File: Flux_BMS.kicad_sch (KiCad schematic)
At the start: 13 parts, among them Q1 BSS84, Q2 BSS84

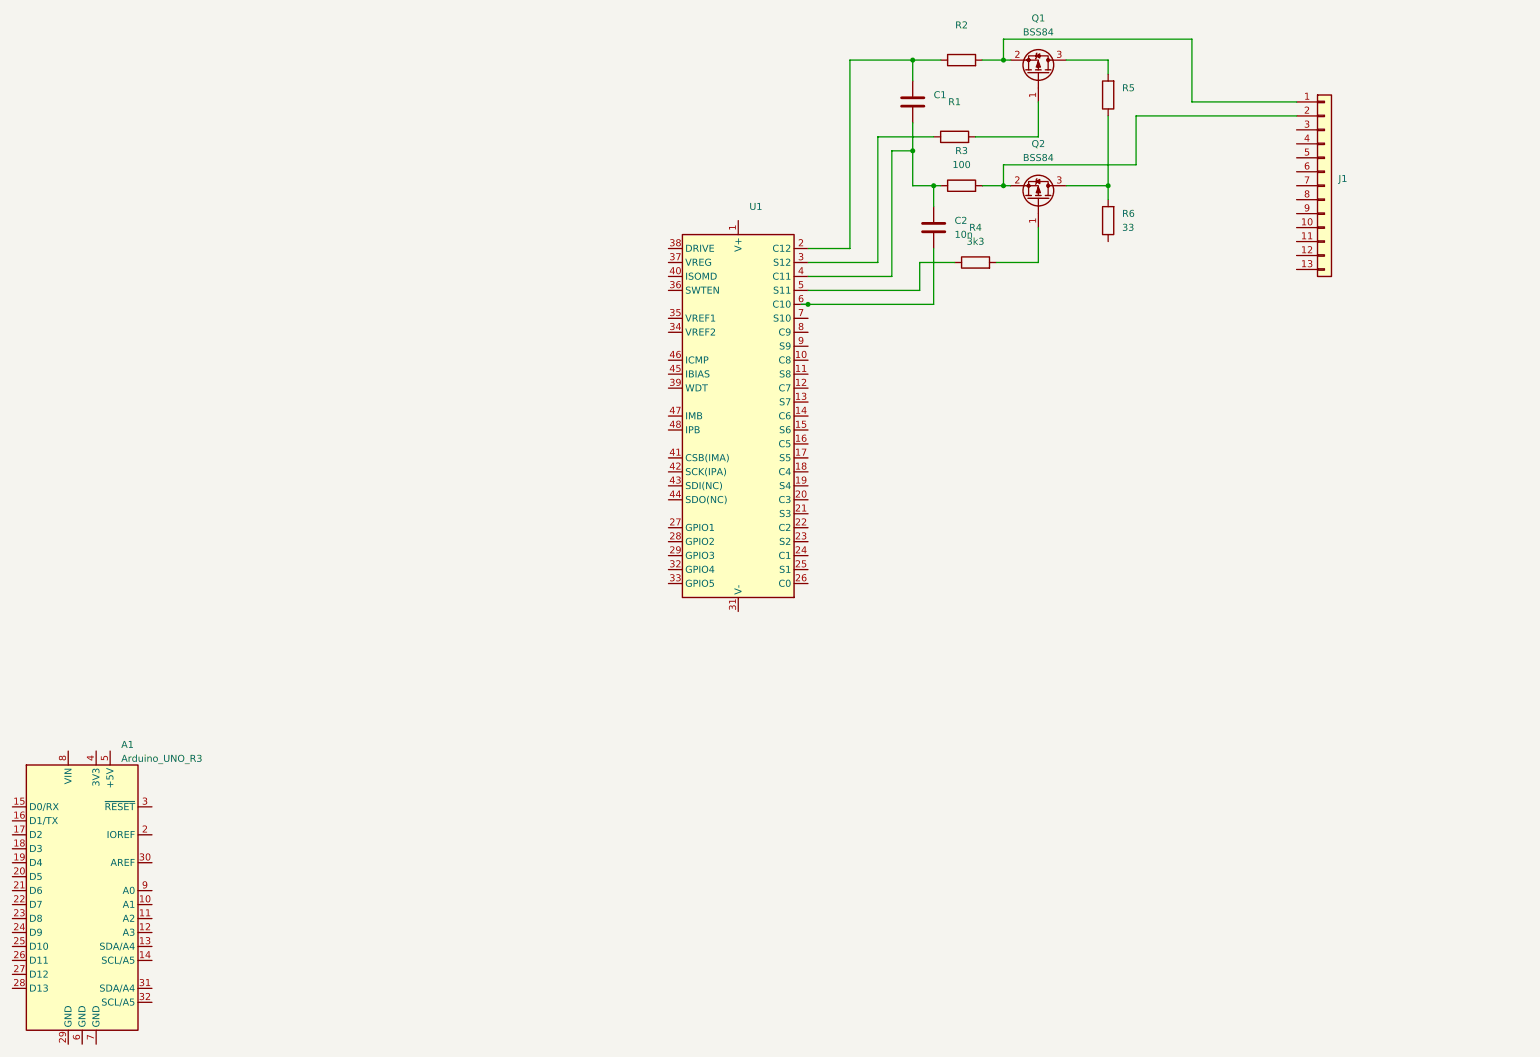
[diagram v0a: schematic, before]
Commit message: Added ltc6811
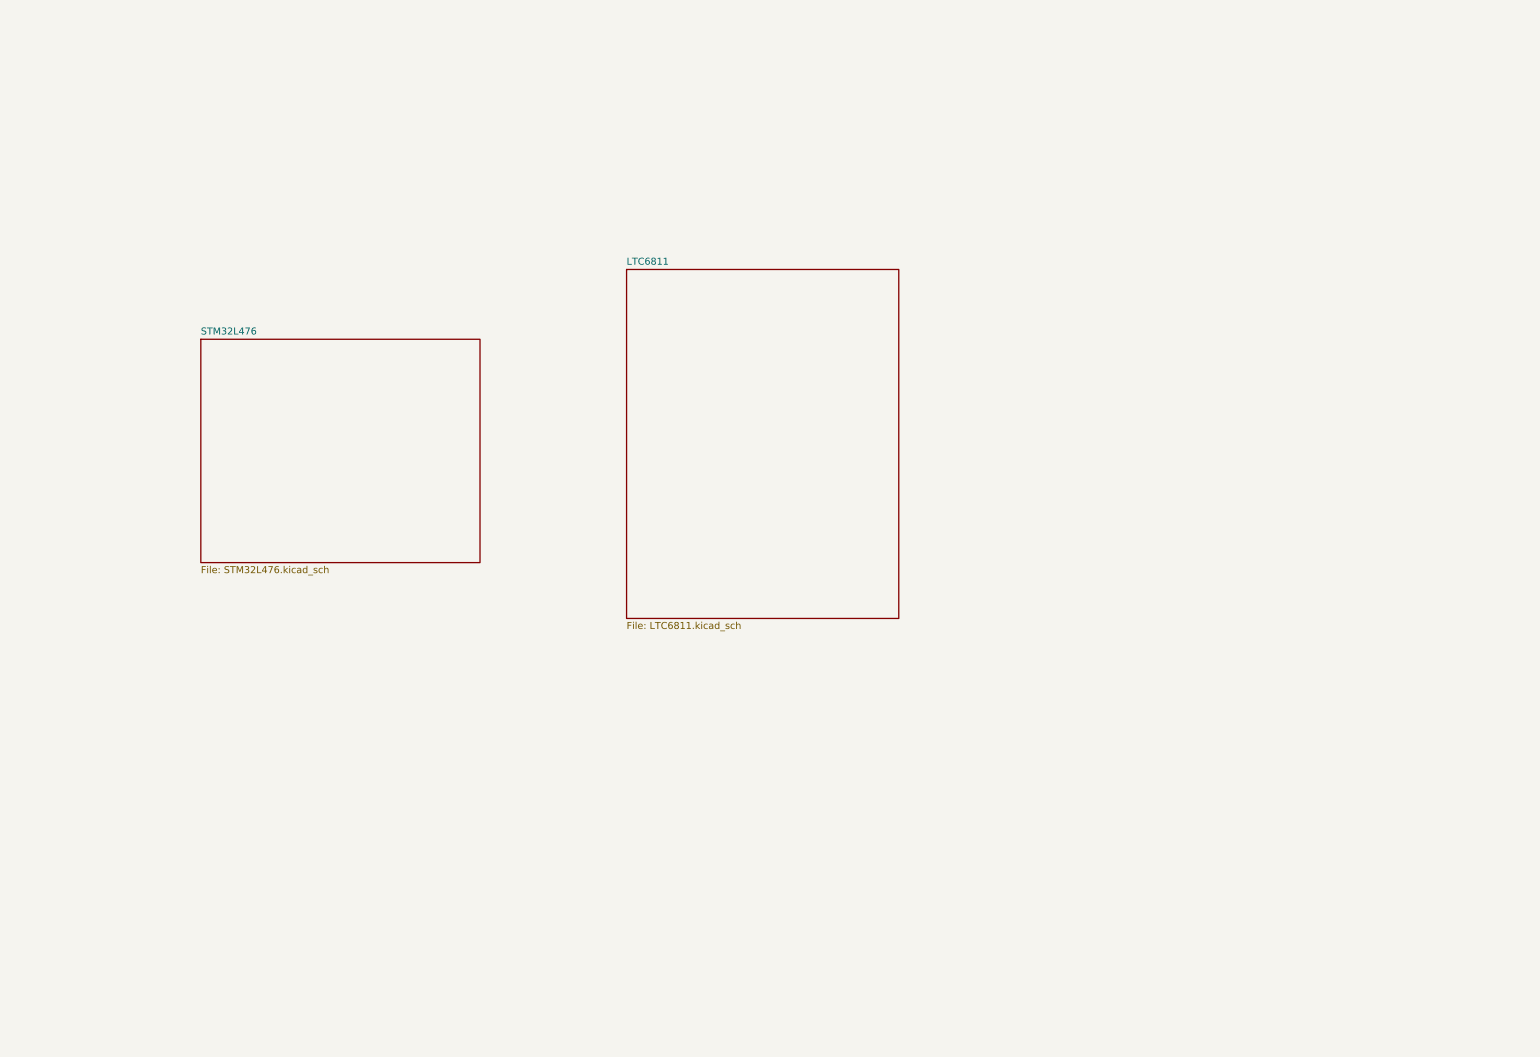
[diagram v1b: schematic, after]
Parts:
- removed A1: Arduino_UNO_R3, Module:Arduino_UNO_R3, symbol MCU_Module:Arduino_UNO_R3
- removed C1: (no value), symbol Device:C
- removed C2: 10n, Capacitor_SMD:C_0805_2012Metric_Pad1.18x1.45mm_HandSolder, symbol Device:C
- removed J1: (no value), symbol Connector_Generic:Conn_01x13
- removed Q1, Q2: BSS84, Package_TO_SOT_SMD:SOT-23, symbol Transistor_FET:BSS84
- removed R1, R5: (no value), Resistor_SMD:R_0805_2012Metric_Pad1.20x1.40mm_HandSolder, symbol Device:R
- removed R2: (no value), symbol Device:R
- removed R3: 100, Resistor_SMD:R_0805_2012Metric_Pad1.20x1.40mm_HandSolder, symbol Device:R
- removed R4: 3k3, Resistor_SMD:R_0805_2012Metric_Pad1.20x1.40mm_HandSolder, symbol Device:R
- removed R6: 33, Resistor_SMD:R_0805_2012Metric_Pad1.20x1.40mm_HandSolder, symbol Device:R
- removed U1: (no value), Package_SO:SSOP-48_5.3x12.8mm_P0.5mm, symbol Battery_Management:LTC6804-1
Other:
- added sheet LTC6811 (LTC6811.kicad_sch)
- added sheet STM32L476 (STM32L476.kicad_sch)

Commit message: Added part of power schematic
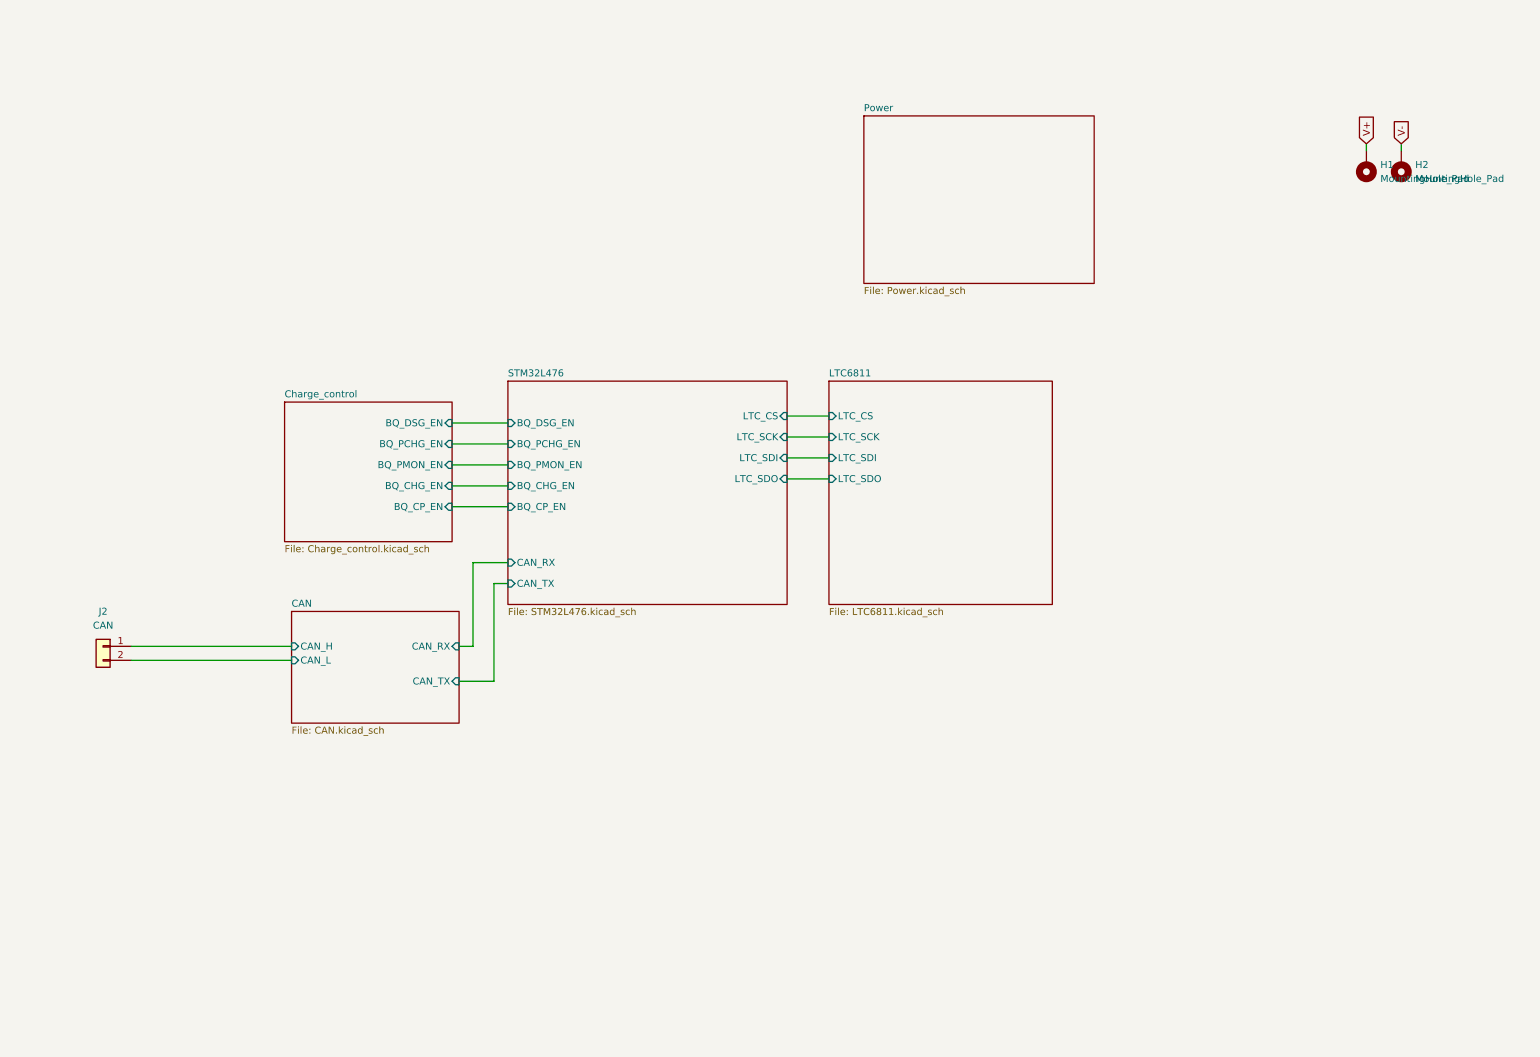
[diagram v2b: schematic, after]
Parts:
- added H1, H2: MountingHole_Pad, MountingHole:MountingHole_2.2mm_M2_DIN965_Pad, symbol Mechanical:MountingHole_Pad
- added J2: CAN, Connector_JST:JST_PH_B2B-PH-K_1x02_P2.00mm_Vertical, symbol Connector_Generic:Conn_01x02
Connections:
- new net CAN/CAN_H: J2.1 (Pin_1)
- new net CAN/CAN_L: J2.2 (Pin_2)
- new net V+: H1.1
- new net V-: H2.1
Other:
- added sheet CAN (CAN.kicad_sch)
- added sheet Charge_control (Charge_control.kicad_sch)
- added sheet Power (Power.kicad_sch)
- sheet LTC6811 ports: added LTC_CS, LTC_SCK, LTC_SDI, LTC_SDO; removed none
- sheet STM32L476 ports: added BQ_CHG_EN, BQ_CP_EN, BQ_DSG_EN, BQ_PCHG_EN, BQ_PMON_EN, CAN_RX, CAN_TX, LTC_CS, LTC_SCK, LTC_SDI, LTC_SDO; removed none
